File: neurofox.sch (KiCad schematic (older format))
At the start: 0 parts

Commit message: feat: RC block 2
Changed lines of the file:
@@
 $Descr A4 11693 8268
 encoding utf-8
-Sheet 1 6
+Sheet 1 8
 Title "FOSSASIA - NeuroFox"
 Date "2018-05-31"
@@
 	2975 1095 2975 2400
 Wire Wire Line
-	2975 1415 1660 1415
+	1660 1415 2975 1415
 Connection ~ 1750 1415
 Wire Wire Line
@@
 	2625 1095 2870 1095
 Wire Wire Line
-	2870 1095 2870 2065
-Wire Wire Line
-	2870 2065 4250 2065
+	2870 1095 2870 2525
+$Sheet
+S 3080 1900 710  345
+U 5B10D013
+F0 "Clock Block" 39
+F1 "ClockBlock.sch" 39
+F2 "+5V" I L 3080 1965 39
+F3 "EXCLK" I L 3080 2065 39
+F4 "GND" I L 3080 2165 39
+F5 "CLK" O R 3790 2065 39
+$EndSheet
+Wire Wire Line
+	4150 2065 4150 2525
+Wire Wire Line
+	4150 2525 2870 2525
+Wire Wire Line
+	4250 2065 4150 2065
+Wire Wire Line
+	3990 2065 3990 2160
+Wire Wire Line
+	3990 2160 4250 2160
+Wire Wire Line
+	3790 2065 3990 2065
+Wire Wire Line
+	3080 1965 2870 1965
+Connection ~ 2870 1965
+Wire Wire Line
+	3080 2165 2975 2165
+Connection ~ 2975 2165
+$Sheet
+S 5450 1635 675  430
+U 5B117A7C
+F0 "RC Filter 2" 39
+F1 "RCFilterBlock2.sch" 39
+F2 "OUT1" I L 5450 1985 39
+F3 "OUT2" I L 5450 1890 39
+F4 "OUT3" I L 5450 1800 39
+F5 "OUT4" I L 5450 1710 39
+F6 "OUT1'" O R 6125 1985 39
+F7 "OUT2'" O R 6125 1890 39
+F8 "OUT3'" O R 6125 1800 39
+F9 "OUT4'" O R 6125 1710 39
+$EndSheet
+Wire Wire Line
+	5450 1710 4960 1710
+Wire Wire Line
+	4960 1800 5450 1800
+Wire Wire Line
+	5450 1890 4960 1890
+Wire Wire Line
+	4960 1985 5450 1985
 $EndSCHEMATC

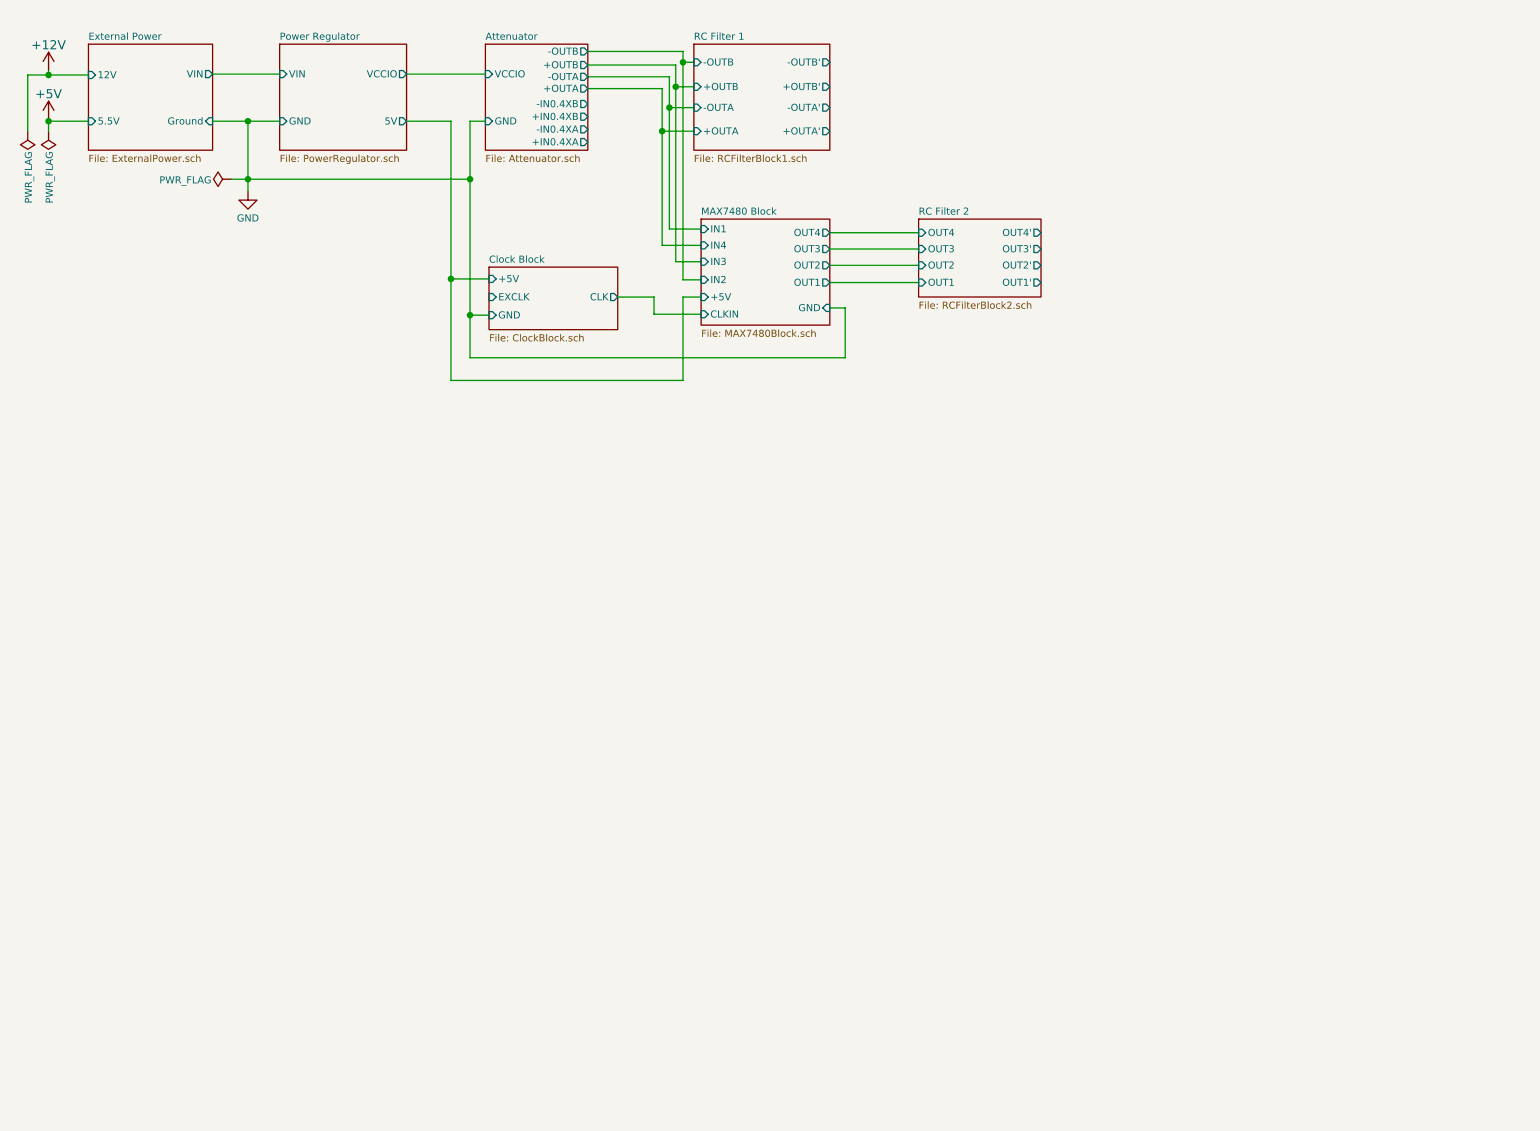
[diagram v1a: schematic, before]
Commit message: feat: added amplifier
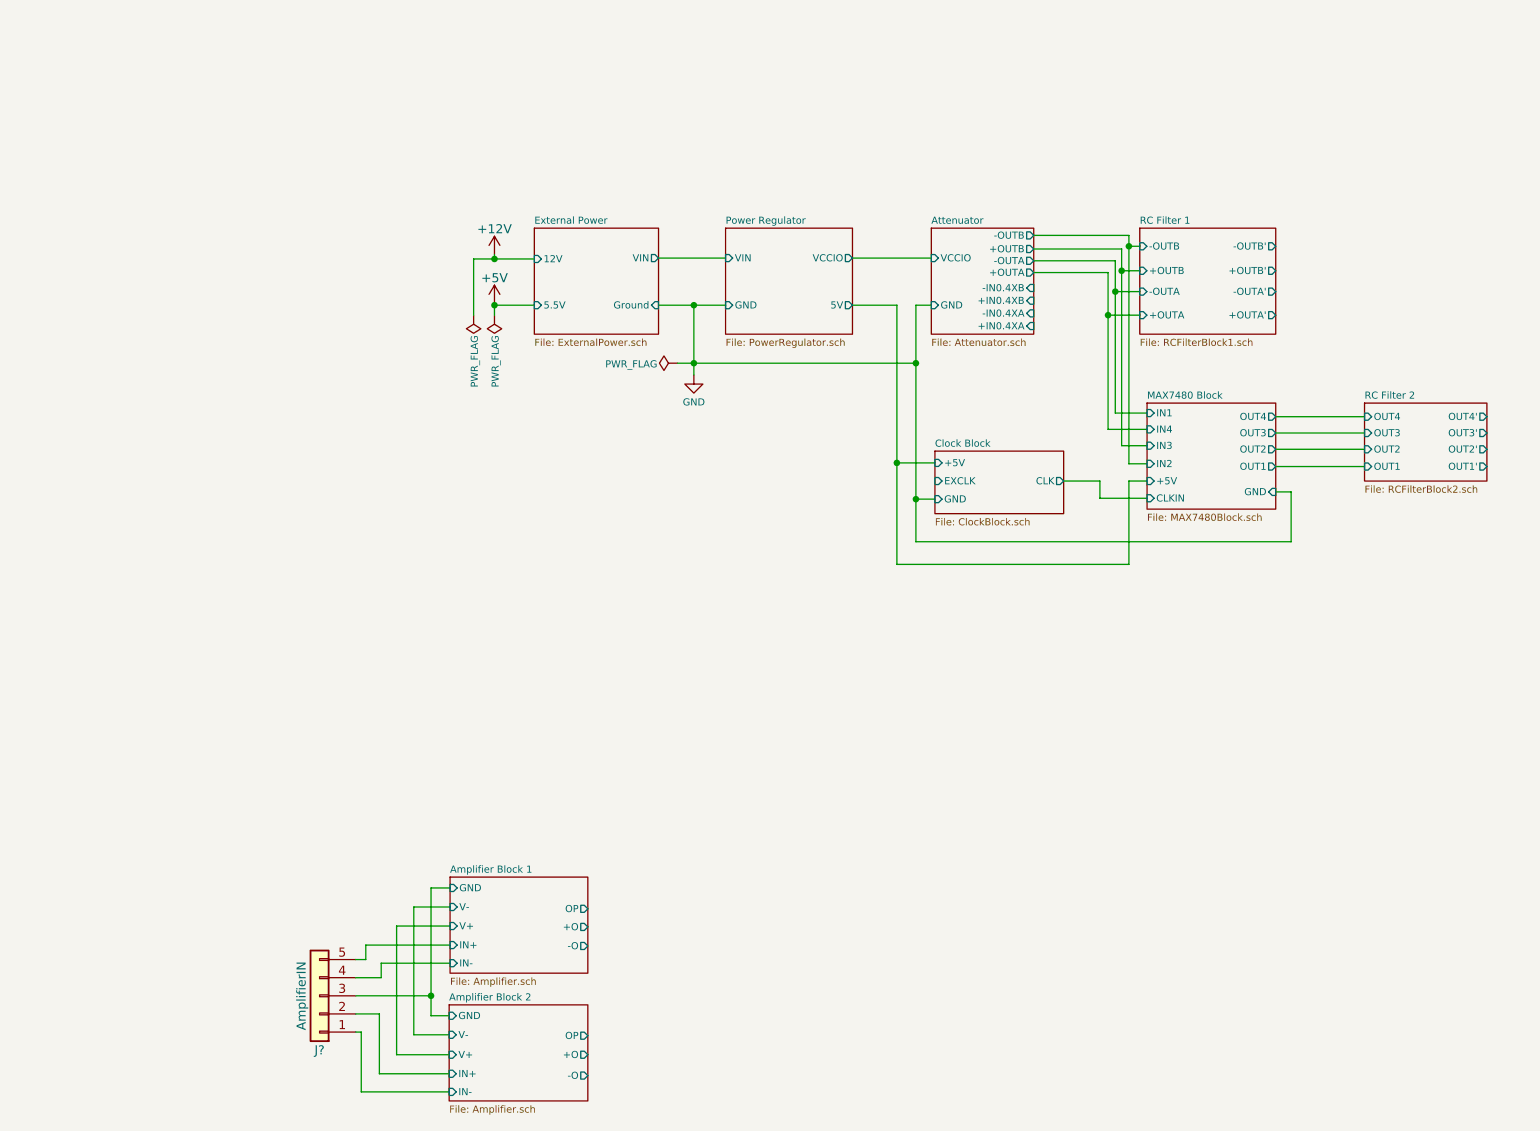
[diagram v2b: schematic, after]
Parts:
- added J?: AmplifierIN, symbol Conn_01x05
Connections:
- new net Amplifier Block 1/GND: J?.3 (Pin_3)
- new net Amplifier Block 1/IN+: J?.5 (Pin_5)
- new net Amplifier Block 1/IN-: J?.4 (Pin_4)
- new net Amplifier Block 2/IN+: J?.2 (Pin_2)
- new net Amplifier Block 2/IN-: J?.1 (Pin_1)

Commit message: feat: alignment
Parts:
- removed J?: AmplifierIN, symbol Conn_01x05
- added J?: Channel, symbol Conn_01x04_Female
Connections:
- net Amplifier Block 1/IN+: now also J?.4 (Pin_4)
- net Amplifier Block 1/IN-: now also J?.3 (Pin_3)
- net Amplifier Block 2/IN+: now also J?.1 (Pin_1)
- net Amplifier Block 2/IN-: now also J?.2 (Pin_2)
